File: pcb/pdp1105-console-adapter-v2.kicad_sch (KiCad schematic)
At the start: 23 parts, among them J1 SCL Connector, J2 DE9_Plug, Q1 MMBT3904, U1 Pico, U2 MAX3232

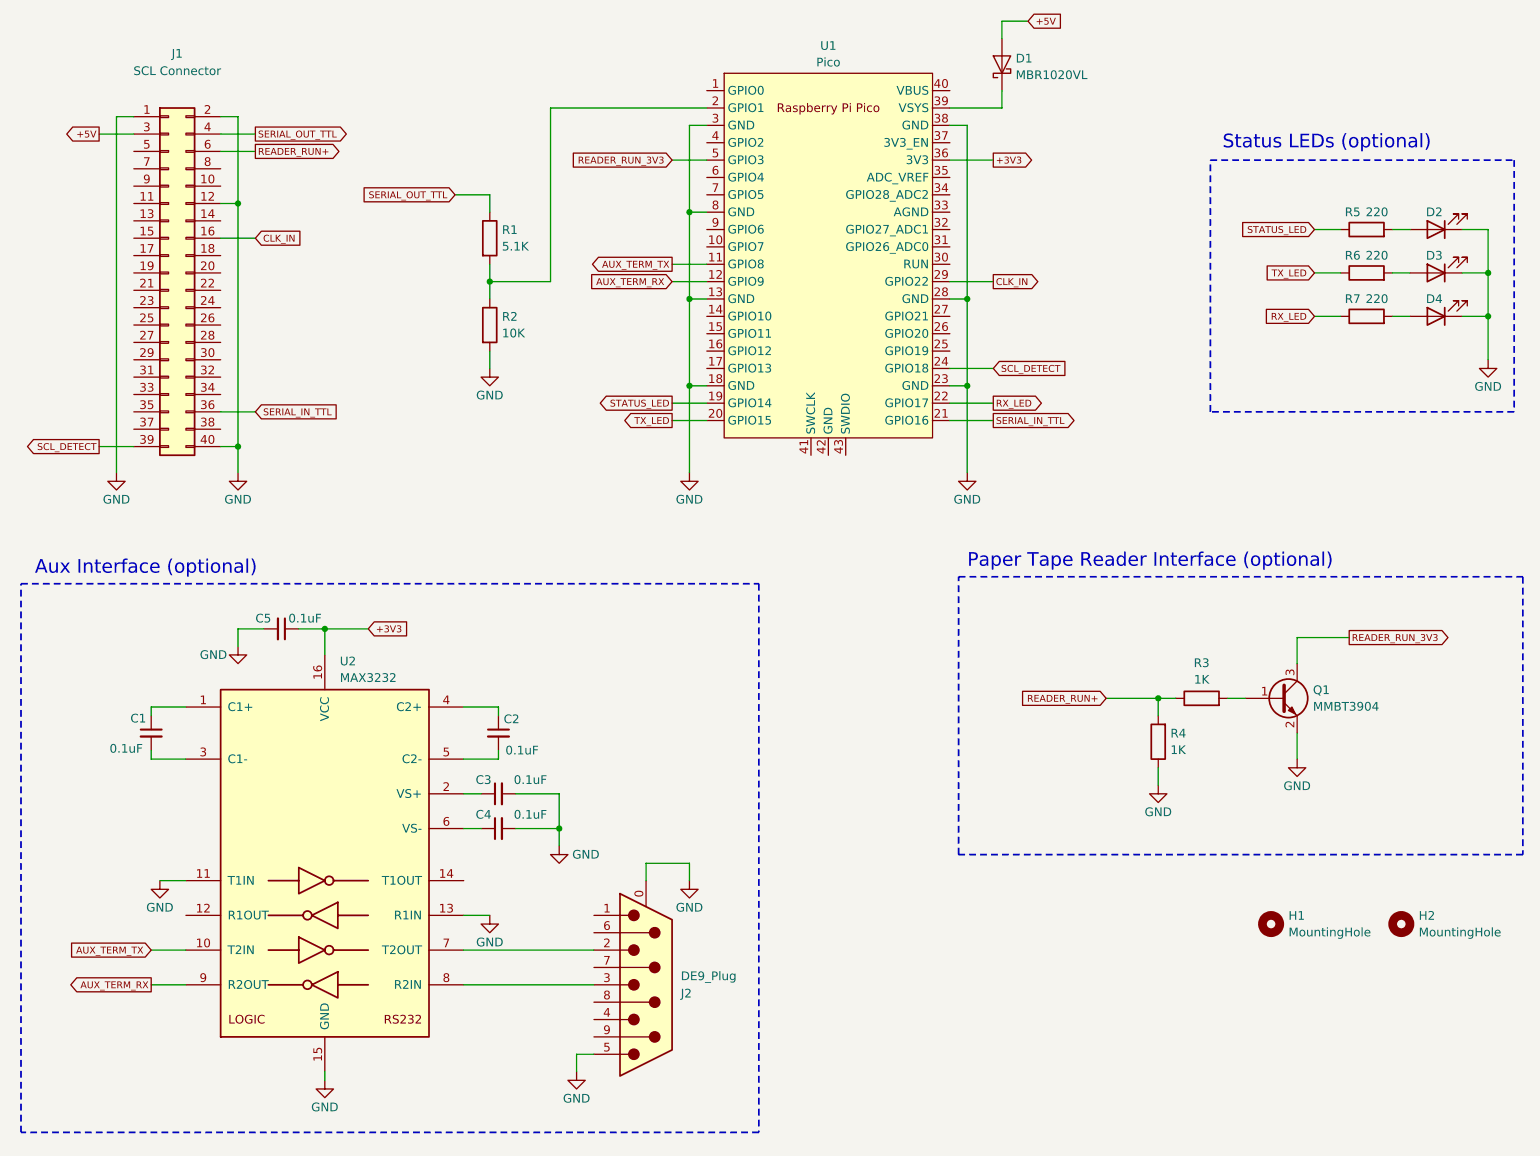
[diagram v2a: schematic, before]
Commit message: Revision 4.1 Schematic and PCB Design
-- Switch to female DE9 connector for Aux port.

-- Added solder jumpers to select between DTE and DCE configuration for Aux
port. Default is set to DCE.

-- Revised LED component layout to allow for copper keep-out area under
Pico W antenna.

-- Added copper ground fill on PCB backside.

-- Cleaned up copper fill on frontside.

-- Made various silkscreen additions to identify part names and orientations.

-- Added PCB layer PDF.

-- Added PCB 3d renderings.
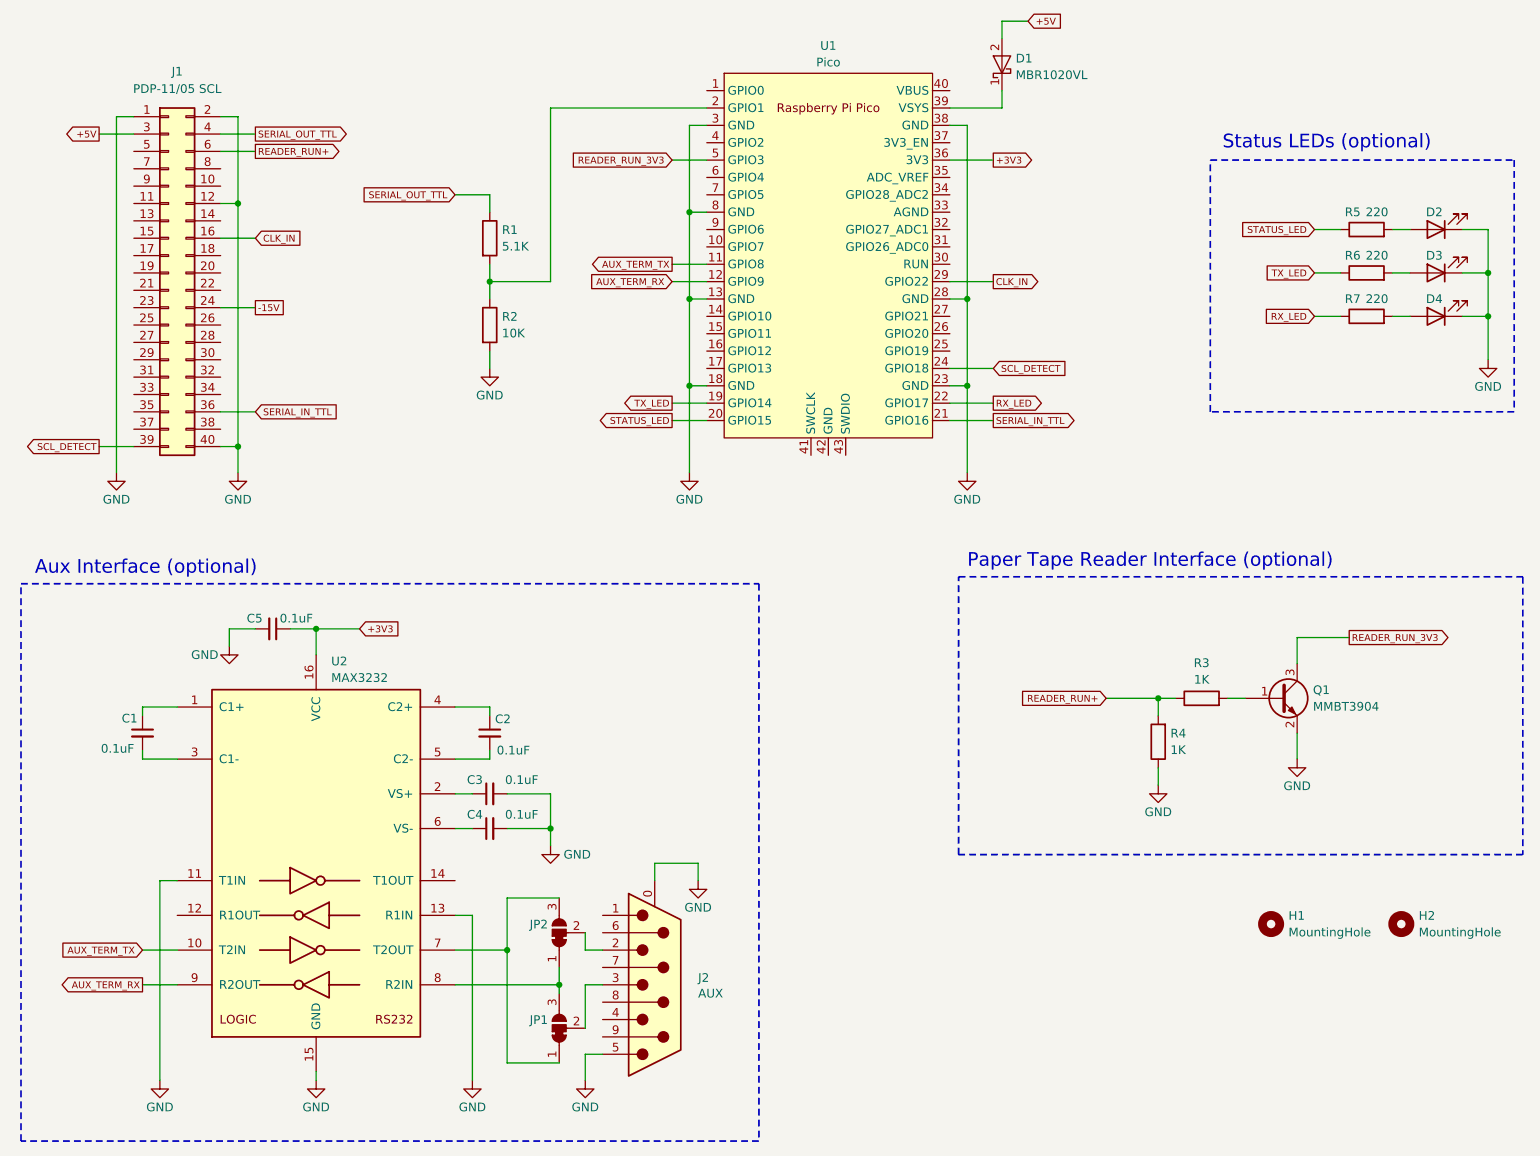
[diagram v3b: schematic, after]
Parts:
- added JP1, JP2: SolderJumper_3_Bridged12, Jumper:SolderJumper-3_P1.3mm_Bridged12_Pad1.0x1.5mm, symbol Jumper:SolderJumper_3_Bridged12
- J1: value SCL Connector -> PDP-11/05 SCL
- J2: value DE9_Plug -> AUX; footprint Connector_Dsub:DSUB-9_Male_Horizontal_P2.77x2.84mm_EdgePinOffset7.70mm_Housed_MountingHolesOffset9.12mm -> Connector_Dsub:DSUB-9_Female_Horizontal_P2.77x2.84mm_EdgePinOffset7.70mm_Housed_MountingHolesOffset9.12mm
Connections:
- net STATUS_LED: now also U1.20 (GPIO15); no longer U1.19 (GPIO14)
- net TX_LED: now also U1.19 (GPIO14); no longer U1.20 (GPIO15)
- net at U2.7 (T2OUT): now also JP1.1 (A), JP2.3 (B); no longer J2.2
- net at U2.8 (R2IN): now also JP1.3 (B), JP2.1 (A); no longer J2.3
- net -15V: now reaches J1.24 (-15V)
- new net: J2.3, JP1.2 (C)
- new net: J2.2, JP2.2 (C)
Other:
- moved on the sheet: C1, C2, C3, C4, C5, J2, U2

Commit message: ﻿Revision 4.2 Schematic and PCB Design
-- Fixed bug in schematic that resulted in the AUX port defaulting to DTE
configuration instead of DCE.

-- Fixed bug in PCB silkscreen that mislabeled the jumper configuration for
choosing AUX port DTE vs. DCE configuration.

Note that revision 4.2 is firmware compatible with revision 4.1.
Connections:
- net at JP1.1 (A), JP2.3 (B): now also U2.8 (R2IN); no longer U2.7 (T2OUT)
- net at JP1.3 (B), JP2.1 (A): now also U2.7 (T2OUT); no longer U2.8 (R2IN)
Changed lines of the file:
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@@
 	(title_block
 		(title "PDP-11/05 Console Adapter V2")
-		(date "2025-04-12")
-		(rev "4.1")
+		(date "2025-04-19")
+		(rev "4.2")
 		(comment 1 "Licensed under a Creative Commons Attribution 4.0 International License")
 		(comment 2 "Copyright © 2025 Jay Logue")
@@
 		(lib_id "Jumper:SolderJumper_3_Bridged12")
 		(at 116.84 171.45 90)
+		(mirror x)
 		(unit 1)
 		(exclude_from_sim yes)
@@
 		(on_board yes)
 		(dnp no)
-		(fields_autoplaced yes)
 		(property "Reference" "JP1"
-			(at 115.1891 170.2378 90)
+			(at 115.316 170.18 90)
 			(effects
 				(font
@@
 		)
 		(property "Value" "SolderJumper_3_Bridged12"
-			(at 115.1891 172.6621 90)
+			(at 115.1891 170.2379 90)
 			(effects
 				(font
@@
 		(lib_id "Jumper:SolderJumper_3_Bridged12")
 		(at 116.84 157.48 90)
+		(mirror x)
 		(unit 1)
 		(exclude_from_sim yes)
@@
 		(on_board yes)
 		(dnp no)
-		(fields_autoplaced yes)
 		(property "Reference" "JP2"
-			(at 115.1891 156.2678 90)
+			(at 115.316 156.21 90)
 			(effects
 				(font
@@
 		)
 		(property "Value" "SolderJumper_3_Bridged12"
-			(at 115.1891 158.6921 90)
+			(at 115.1891 156.2679 90)
 			(effects
 				(font
